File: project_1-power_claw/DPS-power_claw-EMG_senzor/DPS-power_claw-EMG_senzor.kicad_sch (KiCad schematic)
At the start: 28 parts, among them J1 AudioJack3, J3 Conn_01x03_Pin, U1 LM324, U2 LM324, U3 LM324, U4 LM324

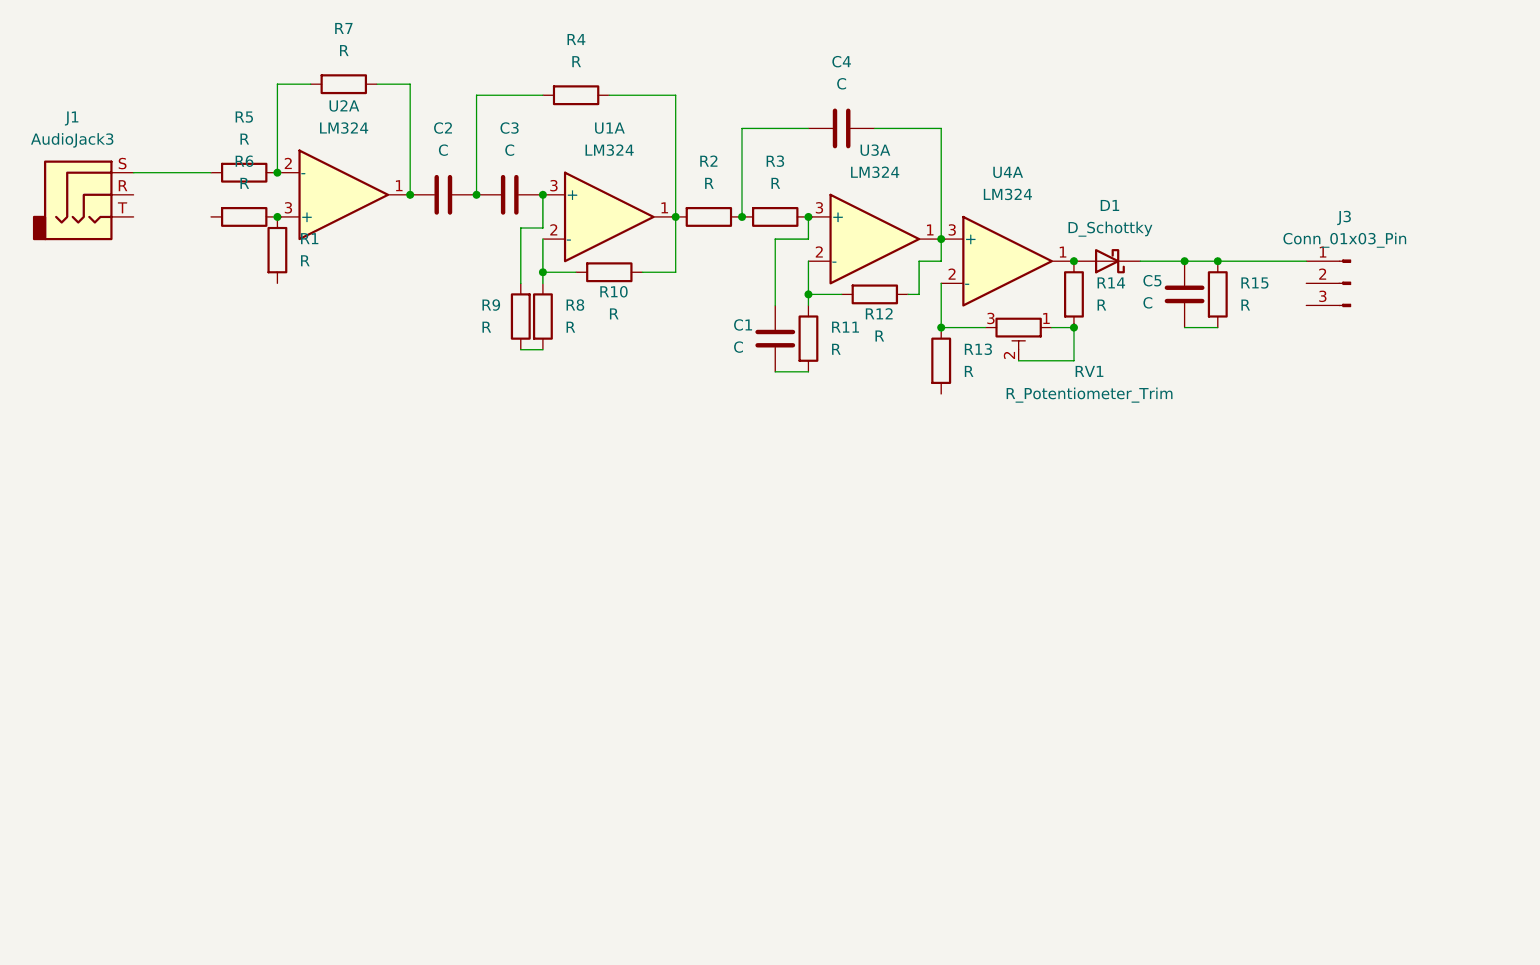
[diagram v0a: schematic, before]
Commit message: finish
EMG modul - finished scheme
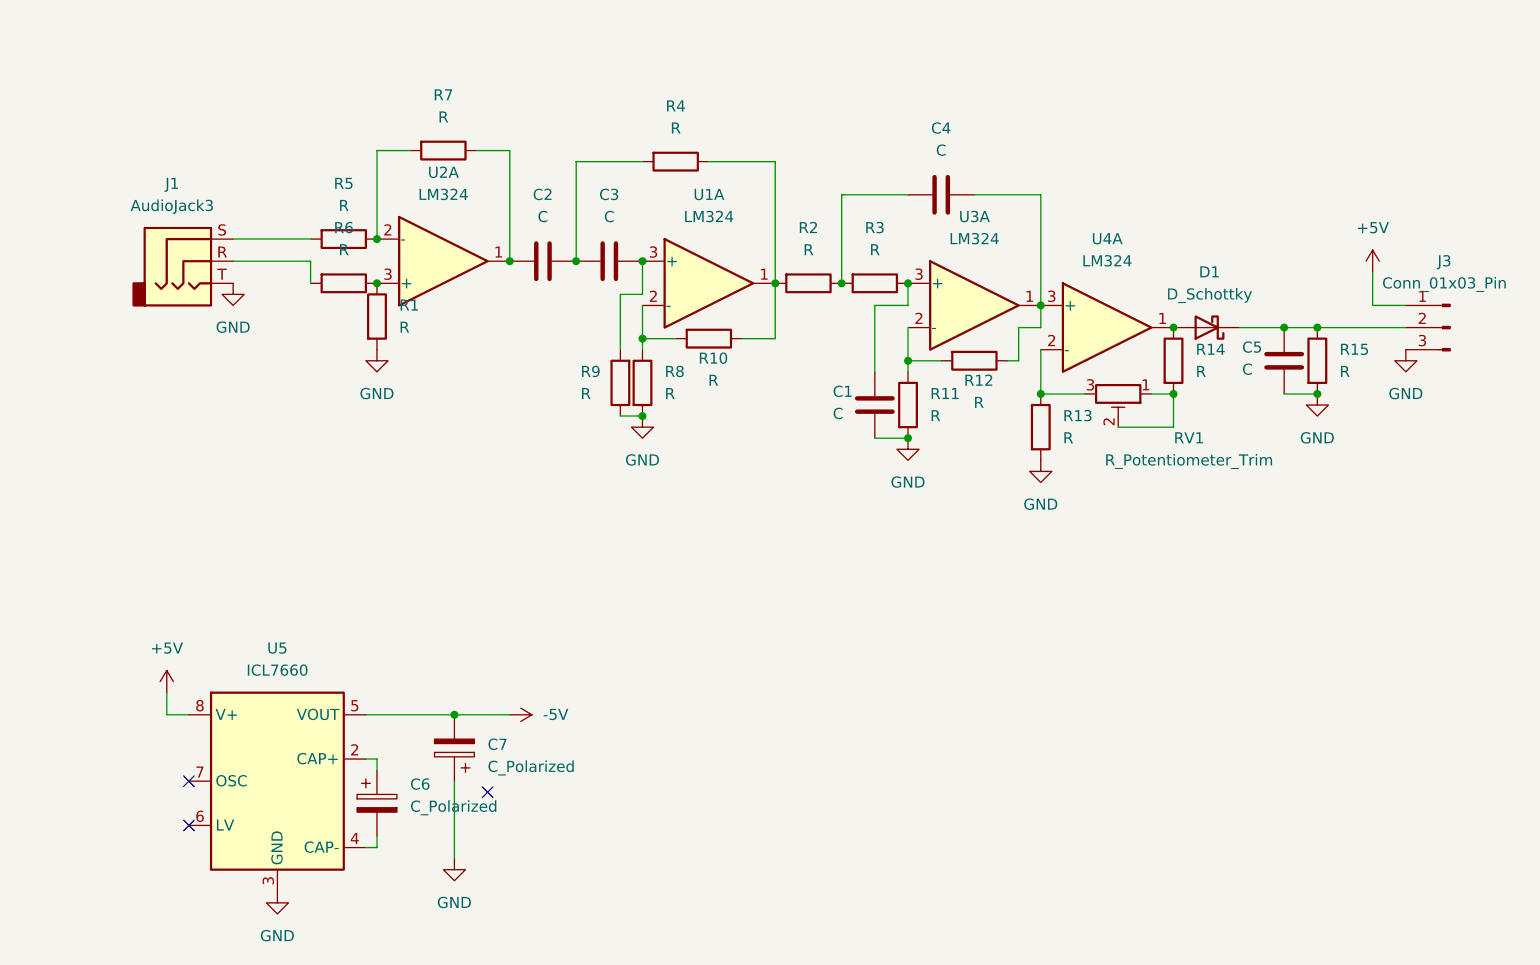
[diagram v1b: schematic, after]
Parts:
- added C6, C7: C_Polarized, symbol Device:C_Polarized
- added U5: ICL7660, symbol Regulator_SwitchedCapacitor:ICL7660
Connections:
- net at C5.1, D1.1 (K), R15.1: now also J3.2 (Pin_2); no longer J3.1 (Pin_1)
- net GND: now reaches C5.2, R15.2
- net GND: now also C1.2, J1.T, J3.3 (Pin_3), R1.2, R11.2, R13.2, R8.2, R9.1, C7.1, U5.3 (GND)
- net at J1.R: now also R6.2
- new net: C6.1, U5.2 (CAP+)
- new net: C6.2, U5.4 (CAP-)
- new net +5V: J3.1 (Pin_1), U5.8 (V+)
- new net -5V: C7.2, U5.5 (VOUT)
- no-connect marks 0 -> 3
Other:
- company: (none) -> Eduard Pokrupa
- title: (none) -> Elektro myo graf
- moved on the sheet: C1, C2, C3, C4, C5, D1, J1, J3, R1, R10, R11, R12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
